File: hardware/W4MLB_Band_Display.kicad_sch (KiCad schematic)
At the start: 18 parts, among them J1 SSW-115-01-G-S, J2 SSW-115-01-G-S, J3 SSQ-108-01-T-D-LL, J4 SAMTEC-TST-108-01-X-D, J5 EJ503B, J6 796683-2, J7 PJRAN1X1U01X, J8 PJRAN1X1U01X, J9 Conn_01x10_Pin, U1 ESP32-DEVKIT-V1

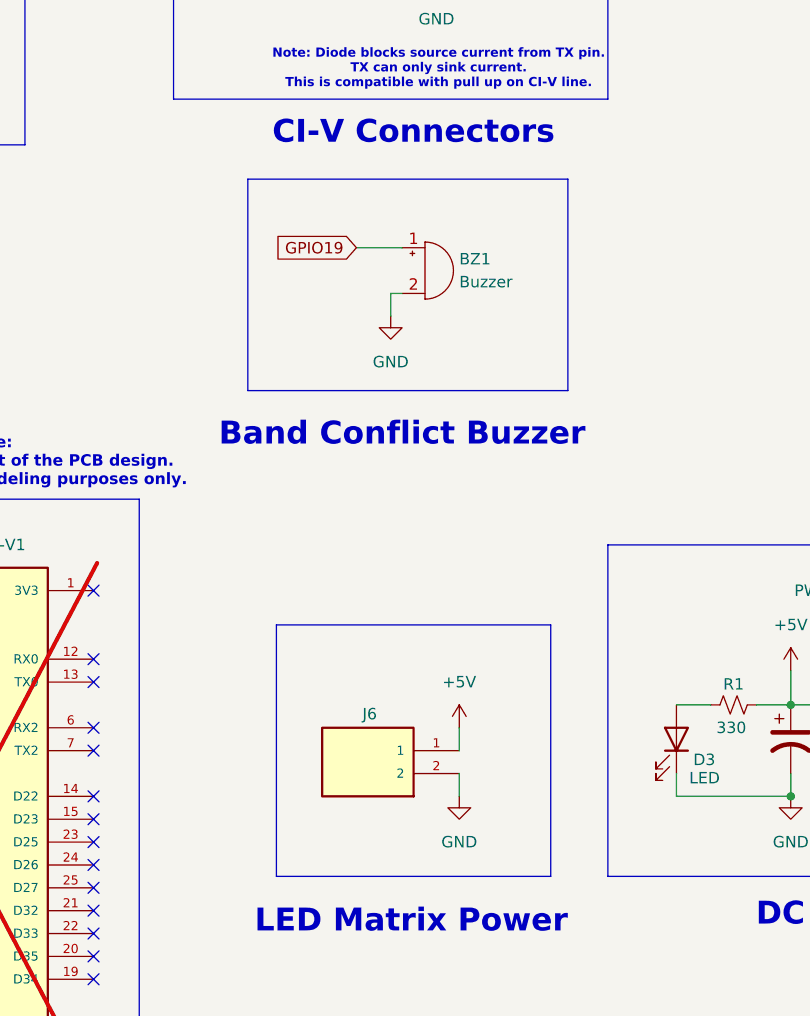
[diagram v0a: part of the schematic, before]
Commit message: Screw terminal connector & Datasheets
Replaced LED Matric power connector with 2 position screw terminal for spade terminals. Also added datasheets for connector parts.
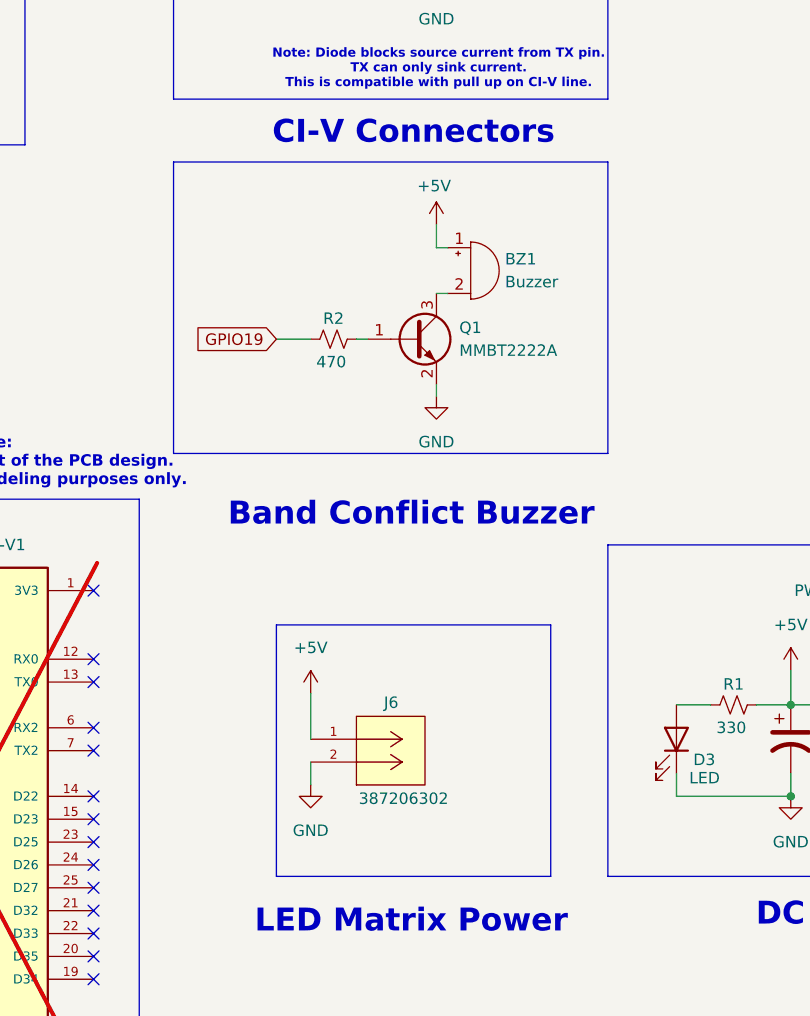
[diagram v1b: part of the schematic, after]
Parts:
- removed J6: 796683-2, Footprints:TE_796683-2, symbol 796683-2:796683-2
- added J6: 387206302, Footprints:CONN_SD-38720-002_02_MOL, symbol 387206302:387206302
- added Q1: MMBT2222A, Package_TO_SOT_SMD:SOT-23, symbol Transistor_BJT:MMBT2222A
- added R2: 470, Resistor_SMD:R_0805_2012Metric_Pad1.20x1.40mm_HandSolder, symbol Device:R_Small_US
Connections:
- net +5V: now also BZ1.1 (+), J6.1
- net GND: now also J6.2, Q1.2 (E); no longer BZ1.2 (-)
- net GPIO19: now also R2.1; no longer BZ1.1 (+)
- new net: BZ1.2 (-), Q1.3 (C)
- new net: Q1.1 (B), R2.2
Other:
- moved on the sheet: BZ1

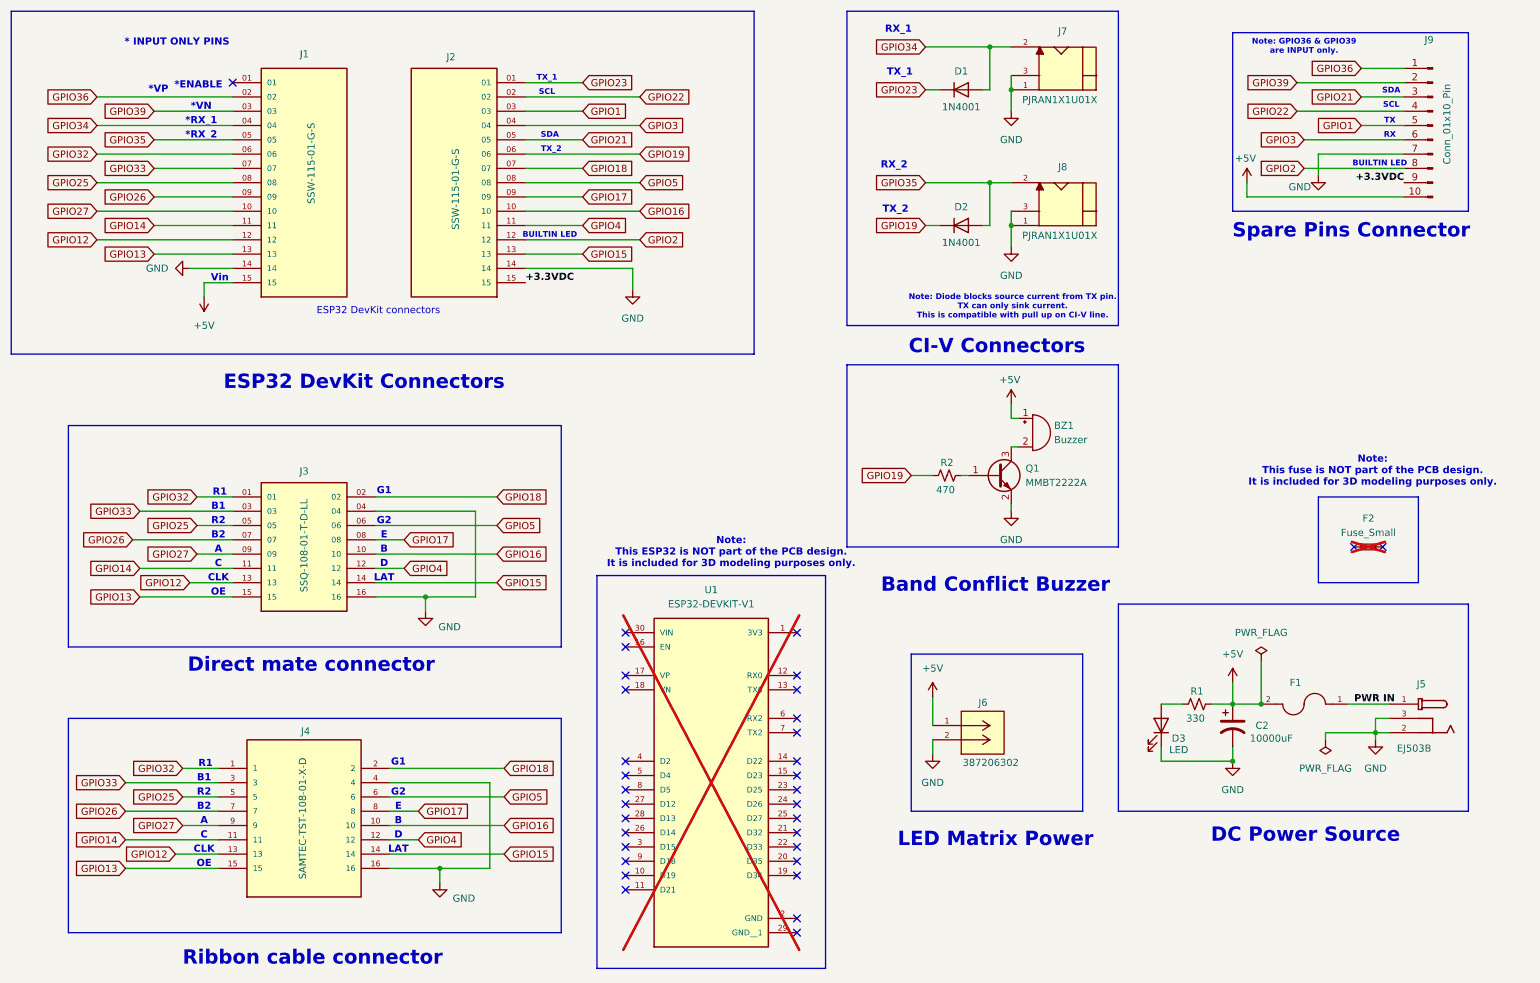
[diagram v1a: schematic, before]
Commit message: Moved Ref Docs & Corrected Buzzer pin
Moved Reference docs from /firmware/libs to Reference Docs at upper level.
Fixed issue where GPIO19 was connected to both TX and Buzzer. Moved buzzer to GPIO2
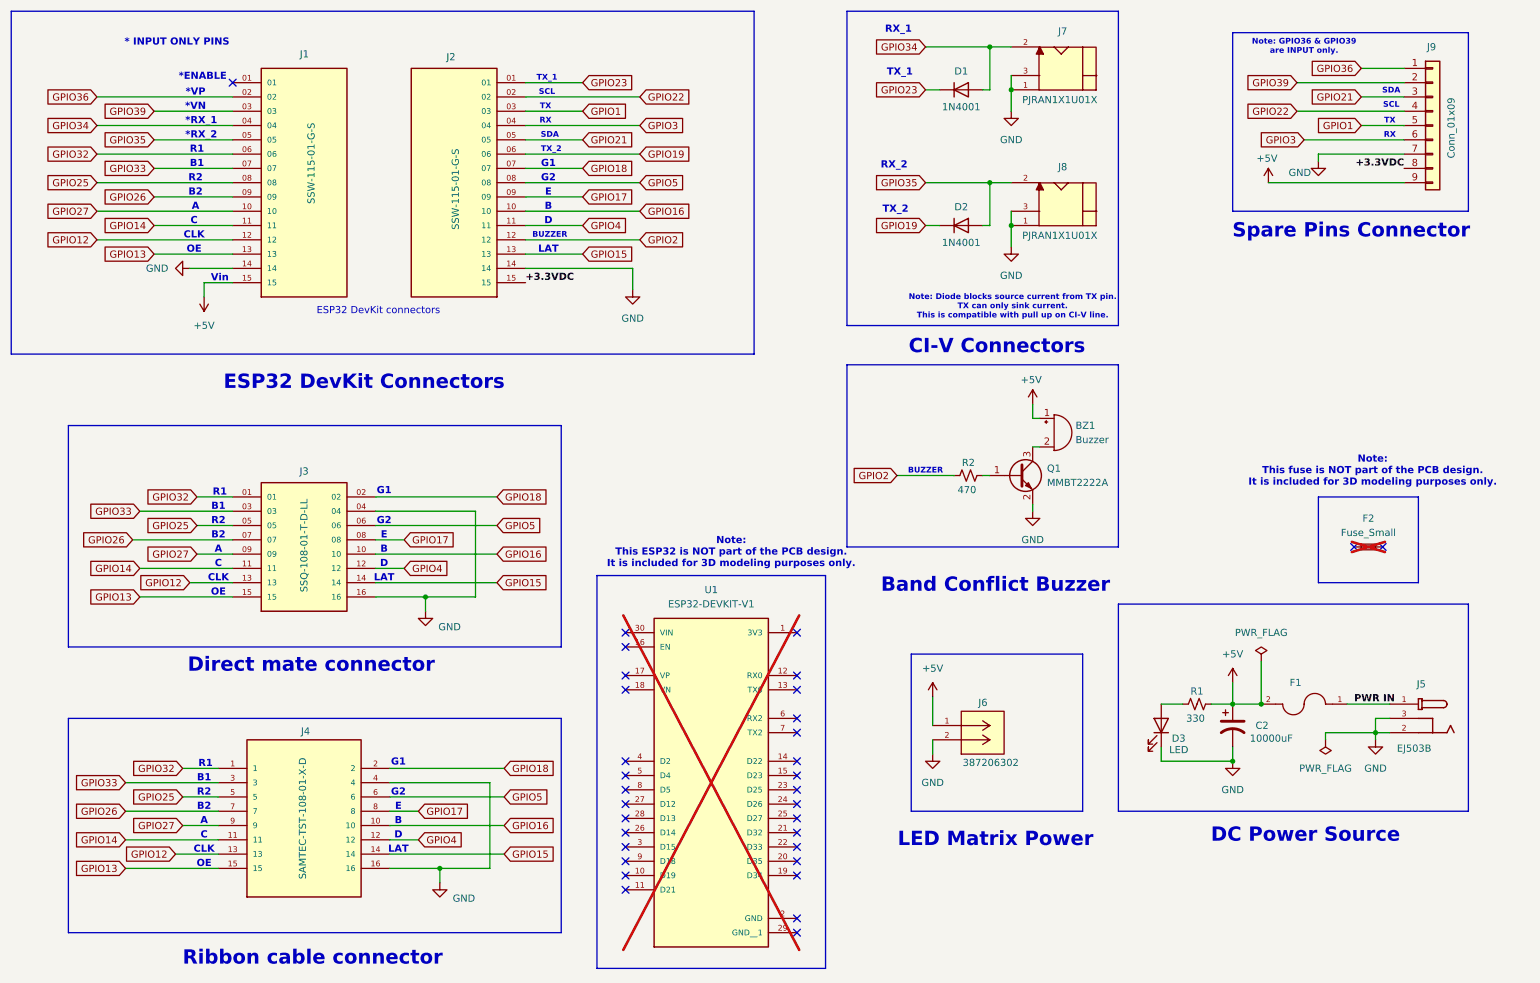
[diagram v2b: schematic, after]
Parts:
- removed J9: Conn_01x10_Pin, Connector_PinSocket_2.54mm:PinSocket_1x10_P2.54mm_Vertical, symbol Connector:Conn_01x10_Pin
- added J9: Conn_01x09, Connector_PinHeader_2.54mm:PinHeader_1x09_P2.54mm_Vertical, symbol Connector_Generic:Conn_01x09
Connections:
- net +3.3VDC: now also J9.8 (Pin_8)
- net +5V: now also J9.9 (Pin_9)
- net GND: now also J9.7 (Pin_7)
- net GPIO1: now also J9.5 (Pin_5)
- net GPIO19: no longer R2.1
- net GPIO2: now also R2.1
- net GPIO21: now also J9.3 (Pin_3)
- net GPIO22: now also J9.4 (Pin_4)
- net GPIO3: now also J9.6 (Pin_6)
- net GPIO36: now also J9.1 (Pin_1)
- net GPIO39: now also J9.2 (Pin_2)
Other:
- note added: "BUZZER"
- note removed: "BUILTIN LED"
- moved on the sheet: BZ1, Q1, R2

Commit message: Smaller terminal block
Changed terminal block to smaller footprint.
Moved PCARS logo to front silkscreen.
Added RF bypass caps to CI-V inputs.
Adjusted location of D1 & D2.
Modified F1 footprint to allow pins 3 &4 to be connected.
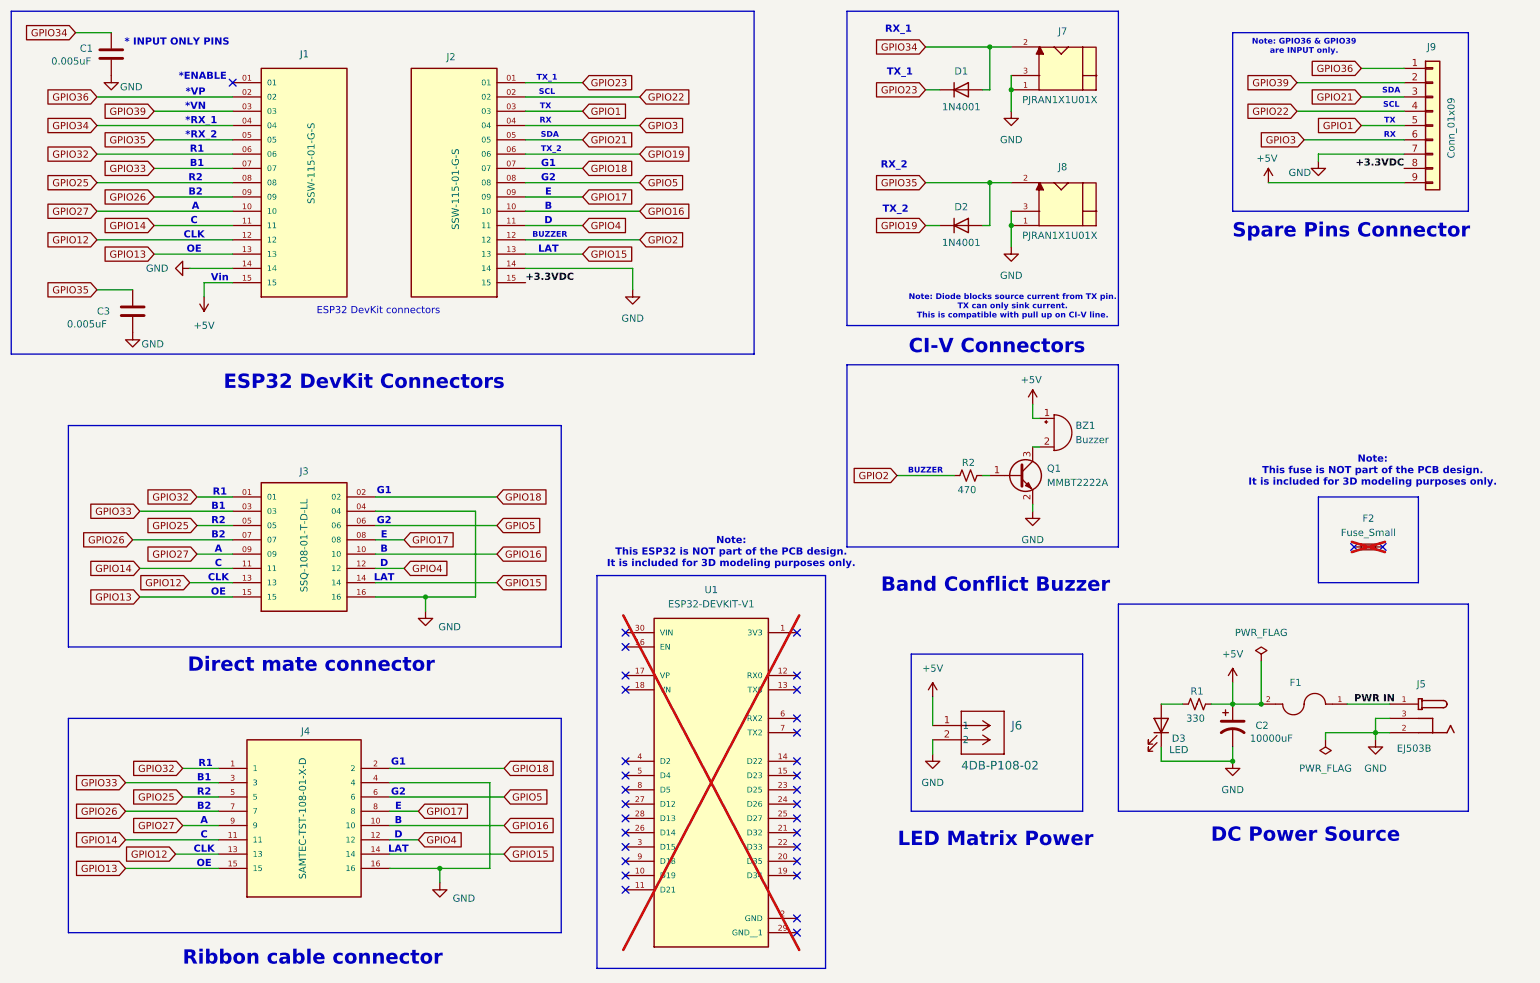
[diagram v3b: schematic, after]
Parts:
- removed J6: 387206302, Footprints:CONN_SD-38720-002_02_MOL, symbol 387206302:387206302
- added C1, C3: 0.005uF, Capacitor_SMD:C_0805_2012Metric_Pad1.18x1.45mm_HandSolder, symbol Device:C
- added J6: 4DB-P108-02, Footprints:CONN_4DB-P108-02_TEC, symbol 2025-04-21_19-43-31:4DB-P108-02
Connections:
- net +5V: now also J6.1
- net GND: now also C1.2, C3.2, J6.2
- net GPIO34: now also C1.1
- net GPIO35: now also C3.1

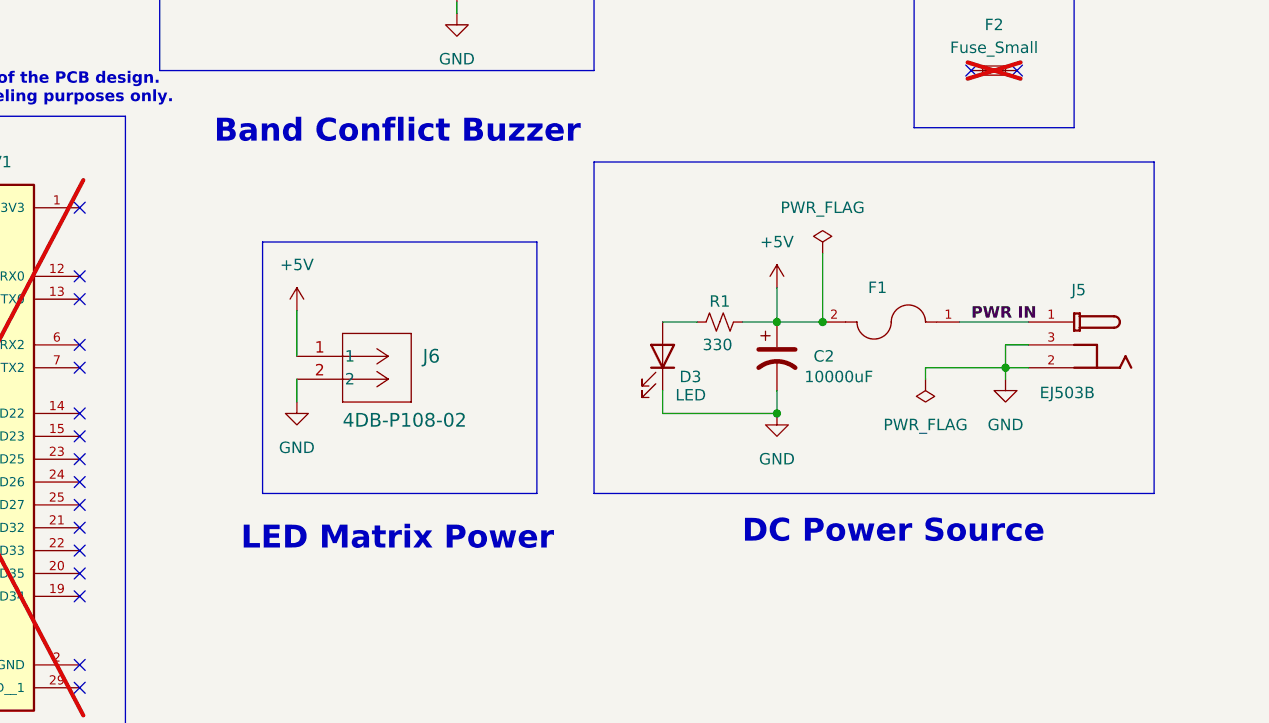
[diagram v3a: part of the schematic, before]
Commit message: Added RF bypass cap to +5V DC supply input.
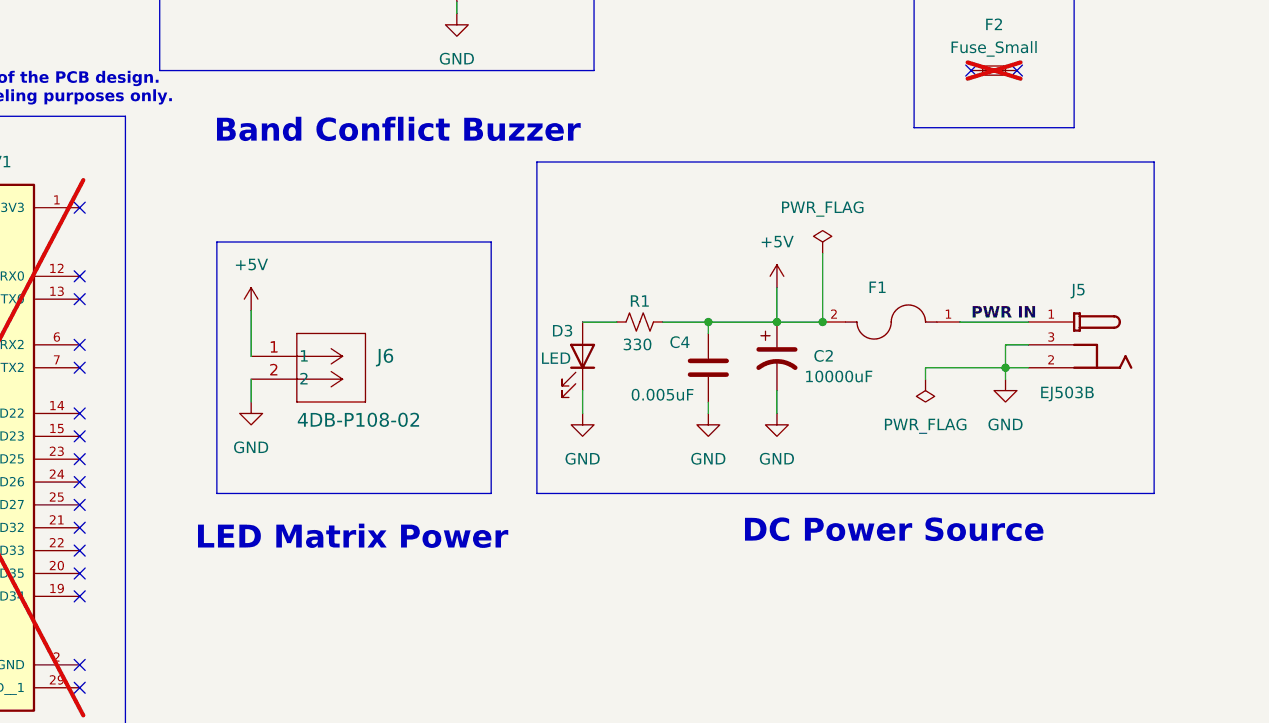
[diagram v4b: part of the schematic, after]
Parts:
- added C4: 0.005uF, Capacitor_SMD:C_0805_2012Metric_Pad1.18x1.45mm_HandSolder, symbol Device:C
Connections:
- net +5V: now also C4.1
- net GND: now also C4.2
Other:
- moved on the sheet: D3, J6, R1
